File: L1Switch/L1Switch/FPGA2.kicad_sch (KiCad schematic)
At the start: 46 parts, among them J10 Conn_02x07_Odd_Even, U1 XC7A35T-FTG256, U10 W25Q128JVS, U11 TXB0108PW, U12 TPS386000RGPR

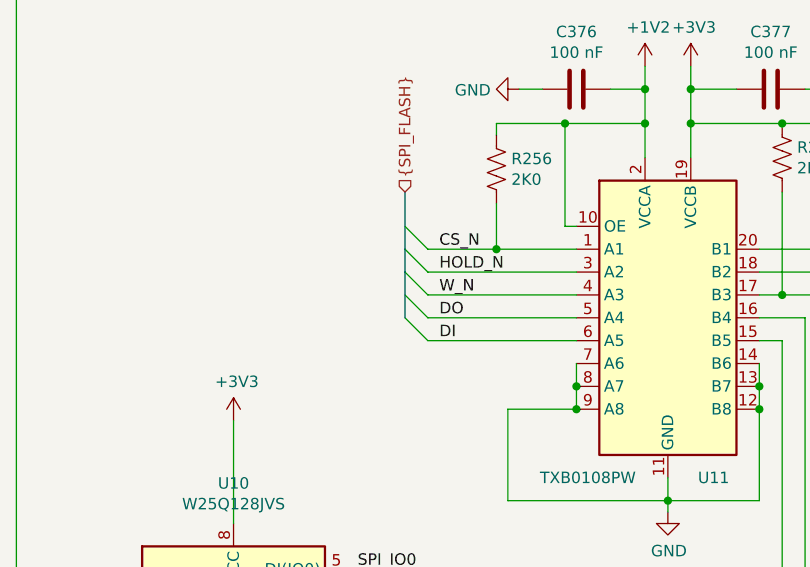
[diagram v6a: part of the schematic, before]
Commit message: Update RJ45 pinout on schematic and partial layout update.
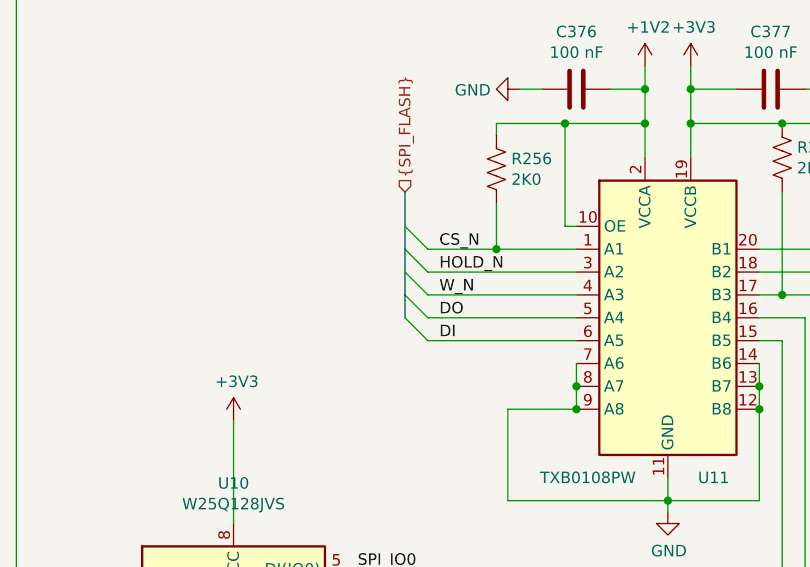
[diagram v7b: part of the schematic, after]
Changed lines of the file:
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@@
 (kicad_sch (version 20200608) (host eeschema "5.99.0-unknown-1973153~101~ubuntu20.04.1")
-  (page 3 12)
+  (page 1 12)
   (paper "B")
   (bus_alias "SPI_FLASH" (members "CS_N" "DI" "DO" "W_N" "HOLD_N"))
@@
   (junction (at 394.97 52.07))
   (no_connect (at 254 41.91))
-  (no_connect (at 316.23 182.88))
   (no_connect (at 233.68 120.65))
-  (no_connect (at 233.68 135.89))
-  (no_connect (at 254 39.37))
-  (no_connect (at 233.68 138.43))
   (no_connect (at 233.68 123.19))
   (no_connect (at 316.23 168.91))
+  (no_connect (at 233.68 138.43))
+  (no_connect (at 316.23 182.88))
+  (no_connect (at 254 39.37))
+  (no_connect (at 233.68 135.89))
   (no_connect (at 367.03 148.59))
   (bus_entry (at 347.98 49.53) (size -2.54 -2.54))
@@
     (stroke (width 0) (type solid) (color 0 0 0 0))
   )
-  (bus (pts (xy 345.44 49.53) (xy 345.44 52.07))
-    (stroke (width 0) (type solid) (color 0 0 0 0))
-  )
-  (bus (pts (xy 345.44 52.07) (xy 345.44 57.15))
-    (stroke (width 0) (type solid) (color 0 0 0 0))
-  )
+  (bus (pts (xy 345.44 49.53) (xy 345.44 54.61))
+    (stroke (width 0) (type solid) (color 0 0 0 0))
+  )
+  (bus (pts (xy 345.44 54.61) (xy 345.44 57.15))
+    (stroke (width 0) (type solid) (color 0 0 0 0))
+  )

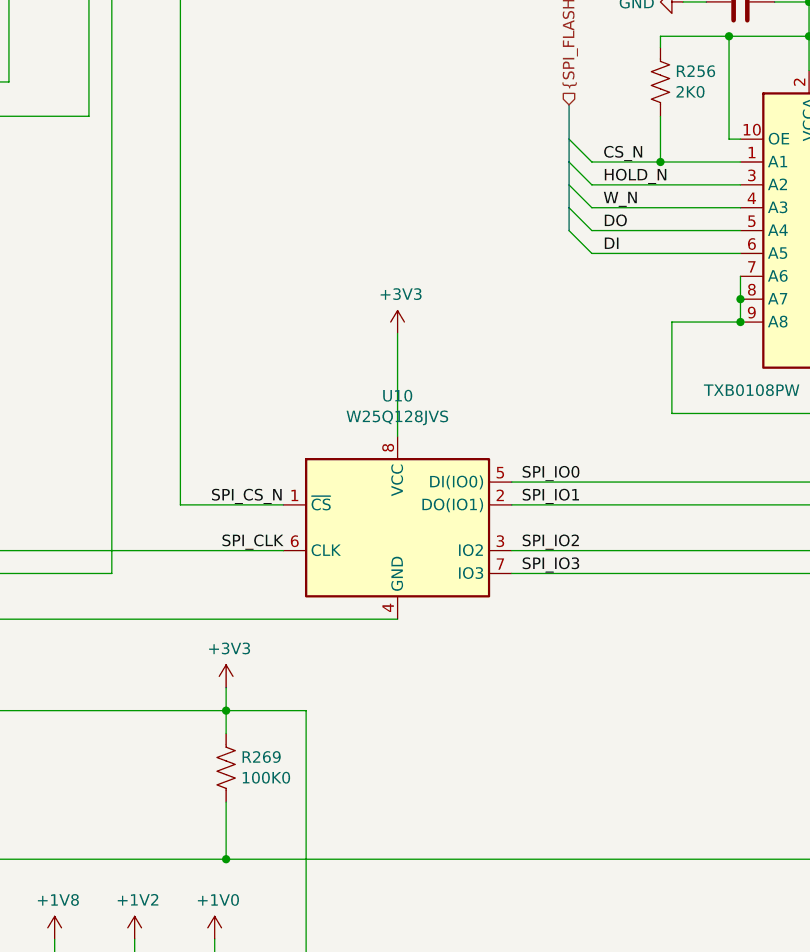
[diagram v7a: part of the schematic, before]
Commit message: Add PWR_FLAG to clean up ERC errors about undriven nets. Change R269 from 100K0 to 10K0.
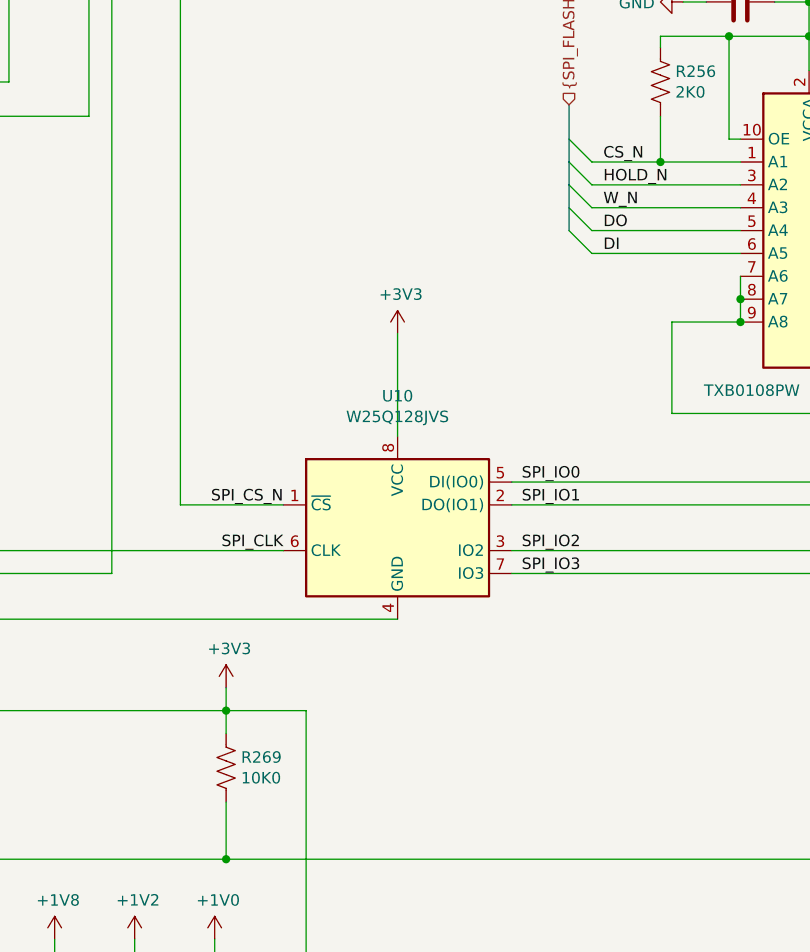
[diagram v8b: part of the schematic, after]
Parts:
- R269: value 100K0 -> 10K0
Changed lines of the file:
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@@
-(kicad_sch (version 20200608) (host eeschema "5.99.0-unknown-1973153~101~ubuntu20.04.1")
-  (page 1 12)
+(kicad_sch (version 20200608) (host eeschema "(5.99.0-1946-g60915fbc7)")
+  (page 3 12)
   (paper "B")
   (bus_alias "SPI_FLASH" (members "CS_N" "DI" "DO" "W_N" "HOLD_N"))
@@
   (junction (at 392.43 207.01))
   (junction (at 394.97 52.07))
+  (no_connect (at 367.03 148.59))
+  (no_connect (at 254 39.37))
   (no_connect (at 254 41.91))
   (no_connect (at 233.68 120.65))
+  (no_connect (at 233.68 135.89))
   (no_connect (at 233.68 123.19))
+  (no_connect (at 316.23 182.88))
+  (no_connect (at 233.68 138.43))
   (no_connect (at 316.23 168.91))
-  (no_connect (at 233.68 138.43))
-  (no_connect (at 316.23 182.88))
-  (no_connect (at 254 39.37))
-  (no_connect (at 233.68 135.89))
-  (no_connect (at 367.03 148.59))
   (bus_entry (at 347.98 49.53) (size -2.54 -2.54))
   (bus_entry (at 347.98 52.07) (size -2.54 -2.54))
@@
     (stroke (width 0) (type solid) (color 0 0 0 0))
   )
-  (bus (pts (xy 345.44 49.53) (xy 345.44 54.61))
-    (stroke (width 0) (type solid) (color 0 0 0 0))
-  )
-  (bus (pts (xy 345.44 54.61) (xy 345.44 57.15))
+  (bus (pts (xy 345.44 49.53) (xy 345.44 52.07))
+    (stroke (width 0) (type solid) (color 0 0 0 0))
+  )
+  (bus (pts (xy 345.44 52.07) (xy 345.44 57.15))
     (stroke (width 0) (type solid) (color 0 0 0 0))
   )
@@
       (effects (font (size 1.27 1.27)) (justify left))
     )
-    (property "Value" "100K0" (id 1) (at 308.9911 117.9893 0)
-      (effects (font (size 1.27 1.27)) (justify left))
-    )
+    (property "Value" "10K0" (id 1) (at 308.9911 117.9893 0)
+      (effects (font (size 1.27 1.27)) (justify left))
+    )
